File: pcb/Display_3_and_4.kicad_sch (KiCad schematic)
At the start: 47 parts, among them Q11 2SA1015, Q12 2SA1015, Q13 2SA1015, Q14 2SA1015, Q15 2SA1015, Q16 2SA1015, Q17 2SA1015, Q18 2SA1015, Q19 2SA1015, Q20 2SA1015, U10 74HC595, U11 4028, U12 LTC-4627JF, U13 LTC-4627JF, U9 74HC595

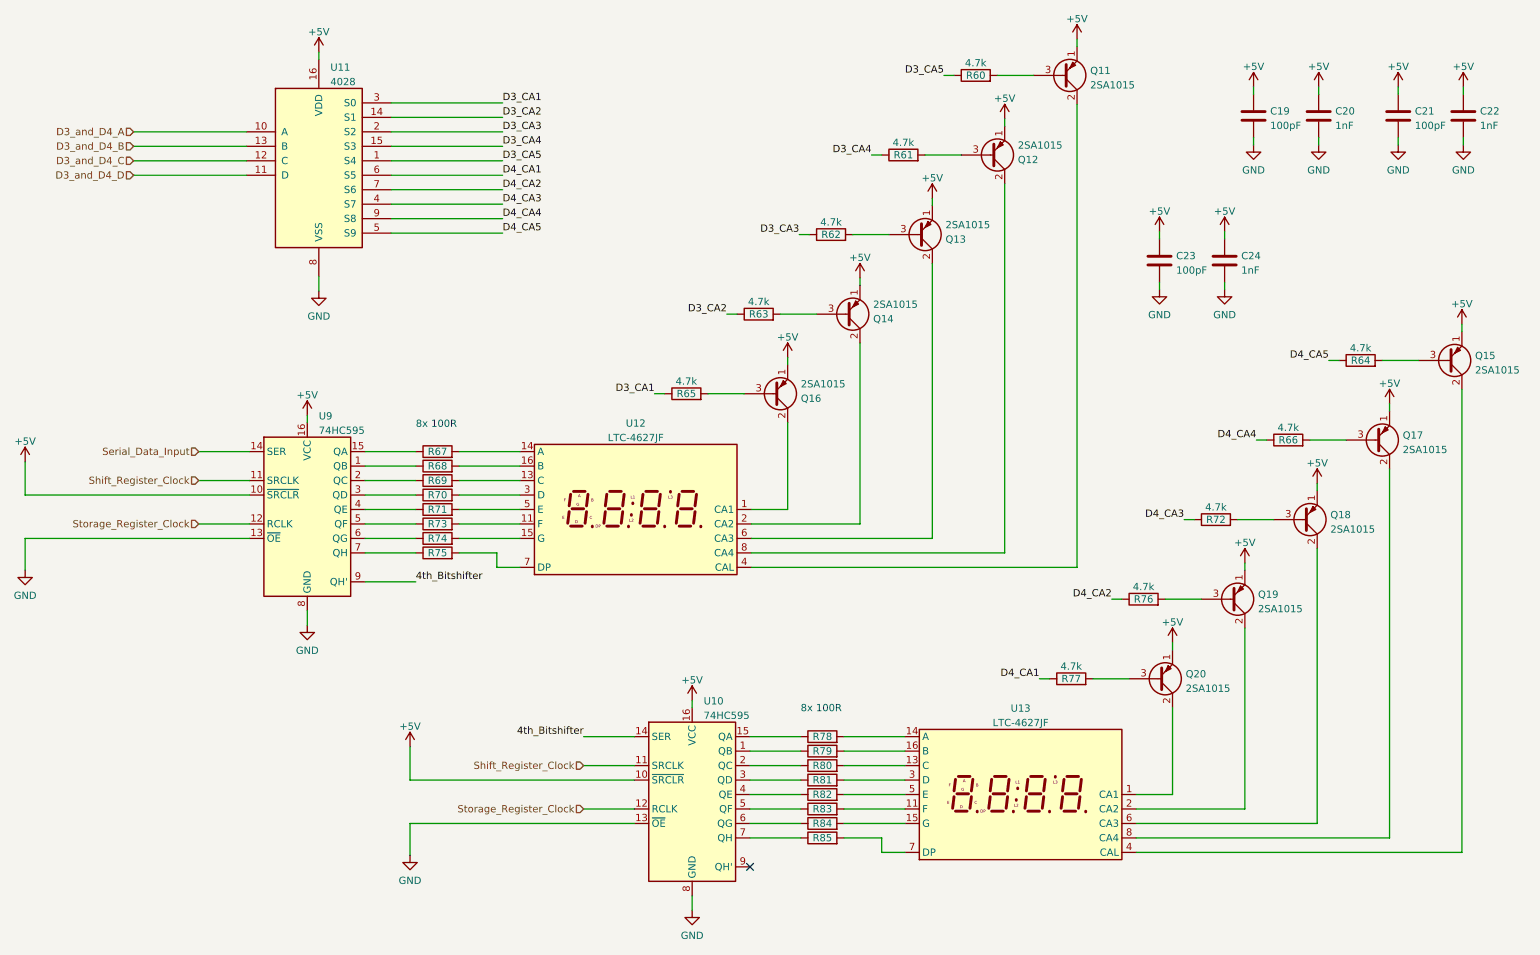
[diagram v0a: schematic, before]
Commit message: reassigned designators and layout progress
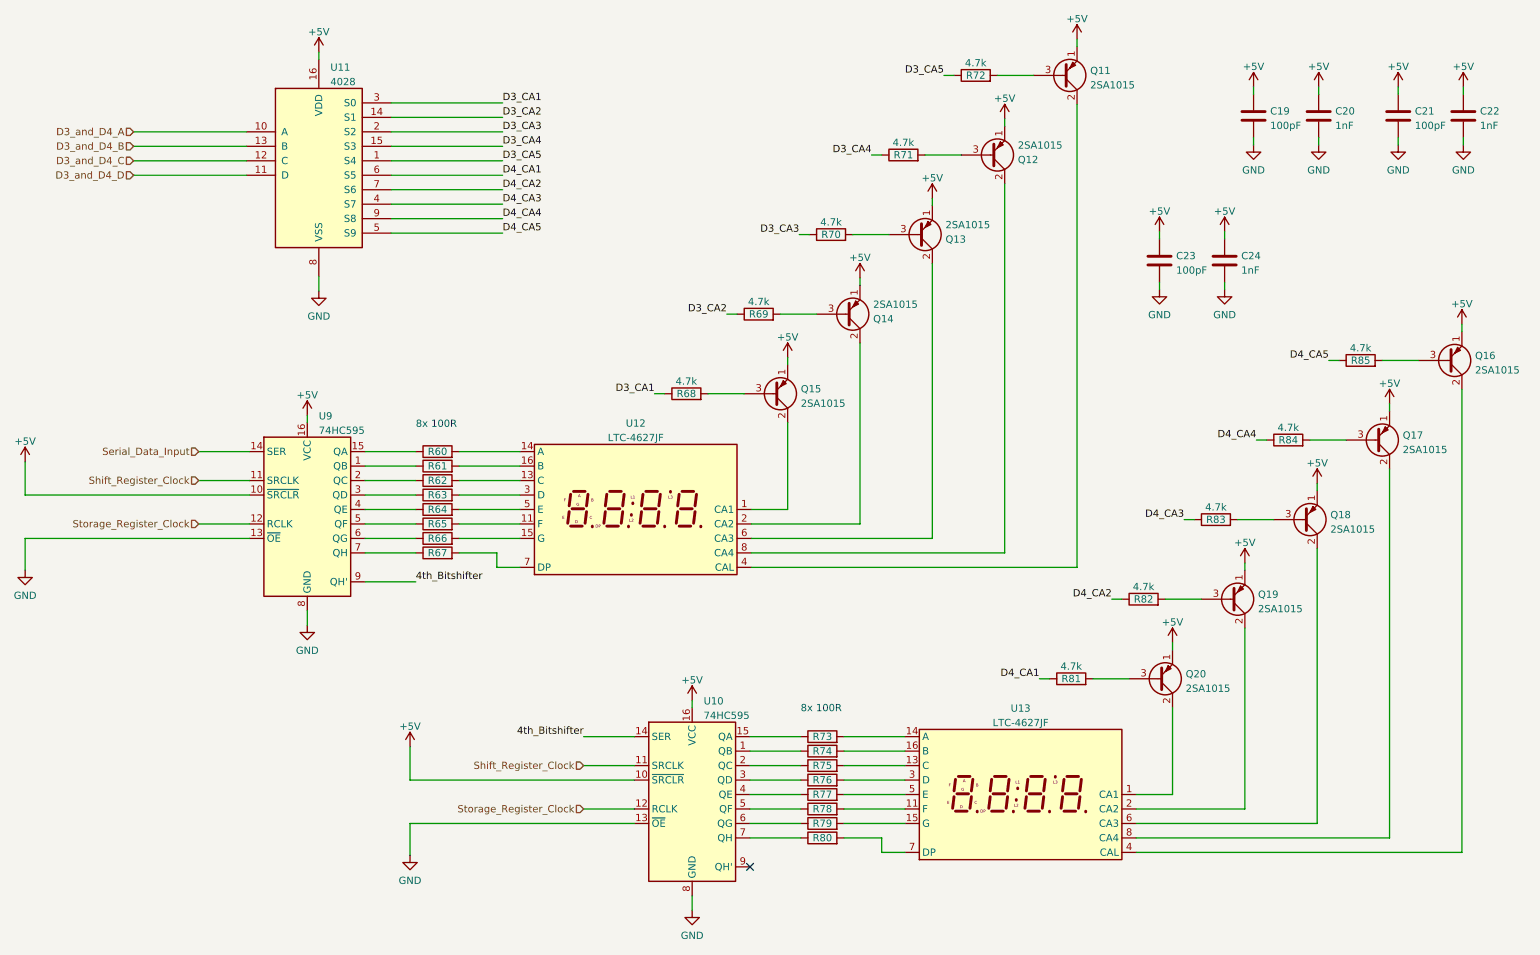
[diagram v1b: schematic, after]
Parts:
- renumbered Q16 to Q15, Q15 to Q16, R67 to R60, R68 to R61, R69 to R62, R70 to R63, R71 to R64, R73 to R65, R74 to R66, R75 to R67, R65 to R68, R63 to R69, R62 to R70, R61 to R71, R60 to R72, R78 to R73, R79 to R74, R80 to R75, R81 to R76, R82 to R77, R83 to R78, R84 to R79, R85 to R80, R77 to R81, R76 to R82, R72 to R83, R66 to R84, R64 to R85

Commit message: new tighter layout
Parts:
- renumbered Q15 to Q11, Q14 to Q12, Q12 to Q14, Q11 to Q15, Q20 to Q16, Q19 to Q17, Q17 to Q19, Q16 to Q20
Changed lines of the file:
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@@
   (symbol (lib_id "Transistor_BJT:2SA1015") (at 148.844 83.312 0) (mirror x) (unit 1)
     (in_bom yes) (on_board yes) (fields_autoplaced)
-    (property "Reference" "Q15" (id 0) (at 153.6954 82.4773 0)
+    (property "Reference" "Q11" (id 0) (at 153.6954 82.4773 0)
       (effects (font (size 1.27 1.27)) (justify left))
     )
@@
   (symbol (lib_id "Transistor_BJT:2SA1015") (at 186.944 41.402 0) (mirror x) (unit 1)
     (in_bom yes) (on_board yes) (fields_autoplaced)
-    (property "Reference" "Q12" (id 0) (at 191.7954 42.2367 0)
-      (effects (font (size 1.27 1.27)) (justify left))
-    )
-    (property "Value" "2SA1015" (id 1) (at 191.7954 39.6998 0)
+    (property "Reference" "Q14" (id 0) (at 191.7954 40.5673 0)
+      (effects (font (size 1.27 1.27)) (justify left))
+    )
+    (property "Value" "2SA1015" (id 1) (at 191.7954 43.1042 0)
       (effects (font (size 1.27 1.27)) (justify left))
     )
@@
   (symbol (lib_id "Transistor_BJT:2SA1015") (at 229.108 119.38 0) (mirror x) (unit 1)
     (in_bom yes) (on_board yes) (fields_autoplaced)
-    (property "Reference" "Q19" (id 0) (at 233.9594 118.5453 0)
+    (property "Reference" "Q17" (id 0) (at 233.9594 118.5453 0)
       (effects (font (size 1.27 1.27)) (justify left))
     )
@@
   (symbol (lib_id "Transistor_BJT:2SA1015") (at 174.244 55.372 0) (mirror x) (unit 1)
     (in_bom yes) (on_board yes) (fields_autoplaced)
-    (property "Reference" "Q13" (id 0) (at 179.0954 56.2067 0)
-      (effects (font (size 1.27 1.27)) (justify left))
-    )
-    (property "Value" "2SA1015" (id 1) (at 179.0954 53.6698 0)
+    (property "Reference" "Q13" (id 0) (at 179.0954 54.5373 0)
+      (effects (font (size 1.27 1.27)) (justify left))
+    )
+    (property "Value" "2SA1015" (id 1) (at 179.0954 57.0742 0)
       (effects (font (size 1.27 1.27)) (justify left))
     )
@@
   (symbol (lib_id "Transistor_BJT:2SA1015") (at 267.208 77.47 0) (mirror x) (unit 1)
     (in_bom yes) (on_board yes) (fields_autoplaced)
-    (property "Reference" "Q16" (id 0) (at 272.0594 76.6353 0)
+    (property "Reference" "Q20" (id 0) (at 272.0594 76.6353 0)
       (effects (font (size 1.27 1.27)) (justify left))
     )
@@
   (symbol (lib_id "Transistor_BJT:2SA1015") (at 216.408 133.35 0) (mirror x) (unit 1)
     (in_bom yes) (on_board yes) (fields_autoplaced)
-    (property "Reference" "Q20" (id 0) (at 221.2594 132.5153 0)
+    (property "Reference" "Q16" (id 0) (at 221.2594 132.5153 0)
       (effects (font (size 1.27 1.27)) (justify left))
     )
@@
   (symbol (lib_id "Transistor_BJT:2SA1015") (at 254.508 91.44 0) (mirror x) (unit 1)
     (in_bom yes) (on_board yes) (fields_autoplaced)
-    (property "Reference" "Q17" (id 0) (at 259.3594 90.6053 0)
+    (property "Reference" "Q19" (id 0) (at 259.3594 90.6053 0)
       (effects (font (size 1.27 1.27)) (justify left))
     )
@@
   (symbol (lib_id "Transistor_BJT:2SA1015") (at 199.644 27.432 0) (mirror x) (unit 1)
     (in_bom yes) (on_board yes) (fields_autoplaced)
-    (property "Reference" "Q11" (id 0) (at 204.4954 26.5973 0)
+    (property "Reference" "Q15" (id 0) (at 204.4954 26.5973 0)
       (effects (font (size 1.27 1.27)) (justify left))
     )
@@
   (symbol (lib_id "Transistor_BJT:2SA1015") (at 161.544 69.342 0) (mirror x) (unit 1)
     (in_bom yes) (on_board yes) (fields_autoplaced)
-    (property "Reference" "Q14" (id 0) (at 166.3954 70.1767 0)
-      (effects (font (size 1.27 1.27)) (justify left))
-    )
-    (property "Value" "2SA1015" (id 1) (at 166.3954 67.6398 0)
-      (effects (font (size 1.27 1.27)) (justify left))
-    )
+    (property "Reference" "Q12" (id 0) (at 166.3954 68.5073 0)
+      (effects (font (size 1.27 1.27)) (justify left))
+    )
+    (property "Value" "2SA1015" (id 1) (at 166.3954 71.0442 0)
+      (effects (font (size 1.27 1.27)) (justify left))
+    )
